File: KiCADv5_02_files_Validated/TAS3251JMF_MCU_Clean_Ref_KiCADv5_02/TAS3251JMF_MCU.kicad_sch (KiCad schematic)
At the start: 0 parts

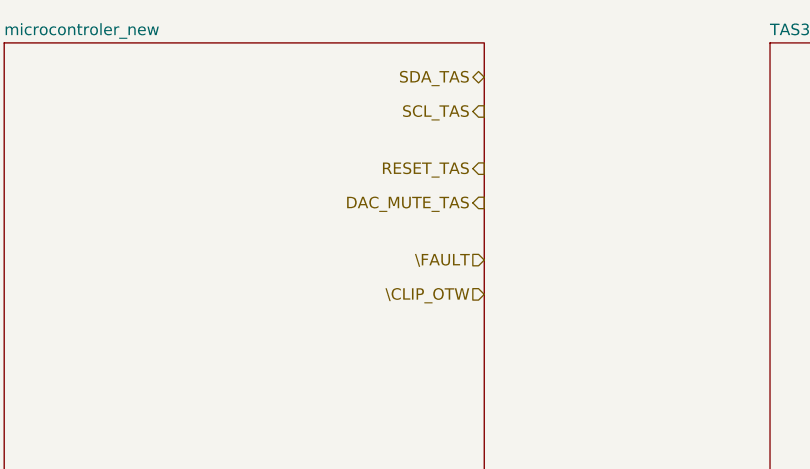
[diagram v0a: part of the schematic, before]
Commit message: Adding signals to control for new uC
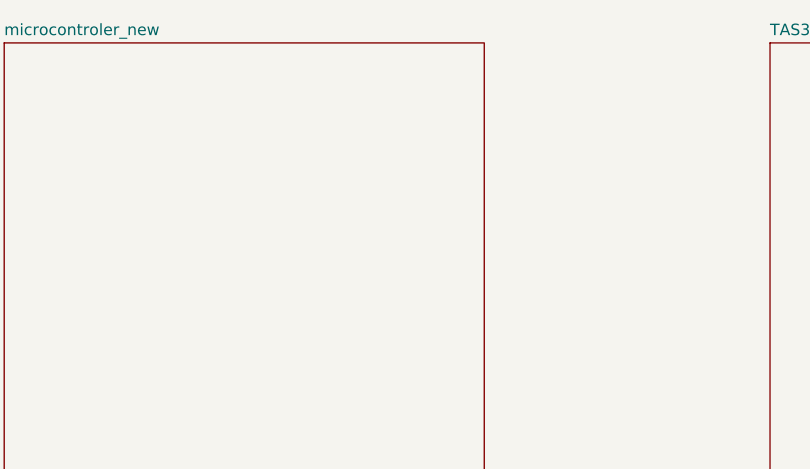
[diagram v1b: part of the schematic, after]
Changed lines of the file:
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@@
 		(comment 1 "Licence: CC BY-SA 4.0")
-	)
-	(hierarchical_label "\\CLIP_OTW"
-		(shape input)
-		(at 186.69 59.69 180)
-		(effects
-			(font
-				(size 1.27 1.27)
-			)
-			(justify right)
-		)
-	)
-	(hierarchical_label "\\FAULT"
-		(shape input)
-		(at 186.69 55.88 180)
-		(effects
-			(font
-				(size 1.27 1.27)
-			)
-			(justify right)
-		)
-	)
-	(hierarchical_label "SCL_TAS"
-		(shape output)
-		(at 186.69 39.37 180)
-		(effects
-			(font
-				(size 1.27 1.27)
-			)
-			(justify right)
-		)
-	)
-	(hierarchical_label "RESET_TAS"
-		(shape output)
-		(at 186.69 45.72 180)
-		(effects
-			(font
-				(size 1.27 1.27)
-			)
-			(justify right)
-		)
-	)
-	(hierarchical_label "SDA_TAS"
-		(shape bidirectional)
-		(at 186.69 35.56 180)
-		(effects
-			(font
-				(size 1.27 1.27)
-			)
-			(justify right)
-		)
-	)
-	(hierarchical_label "DAC_MUTE_TAS"
-		(shape output)
-		(at 186.69 49.53 180)
-		(effects
-			(font
-				(size 1.27 1.27)
-			)
-			(justify right)
-		)
 	)
 	(sheet
